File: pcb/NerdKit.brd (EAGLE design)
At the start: 148.3 x 69.8 mm, 31 parts, among them U2 ARDUINOR3-PINSONLY

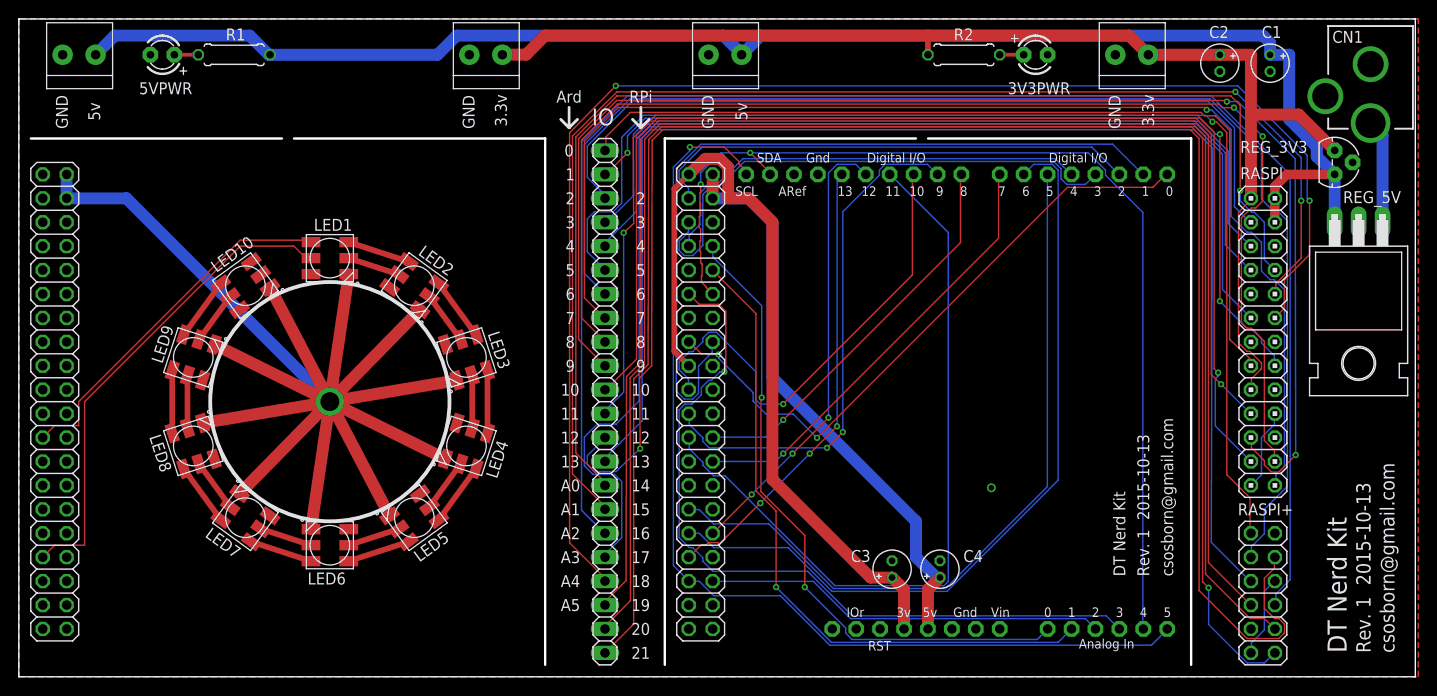
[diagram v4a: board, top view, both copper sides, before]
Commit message: Added OSH Park compliant cutouts for daughter cards.
See http://docs.oshpark.com/submitting-orders/cutouts-and-slots/.
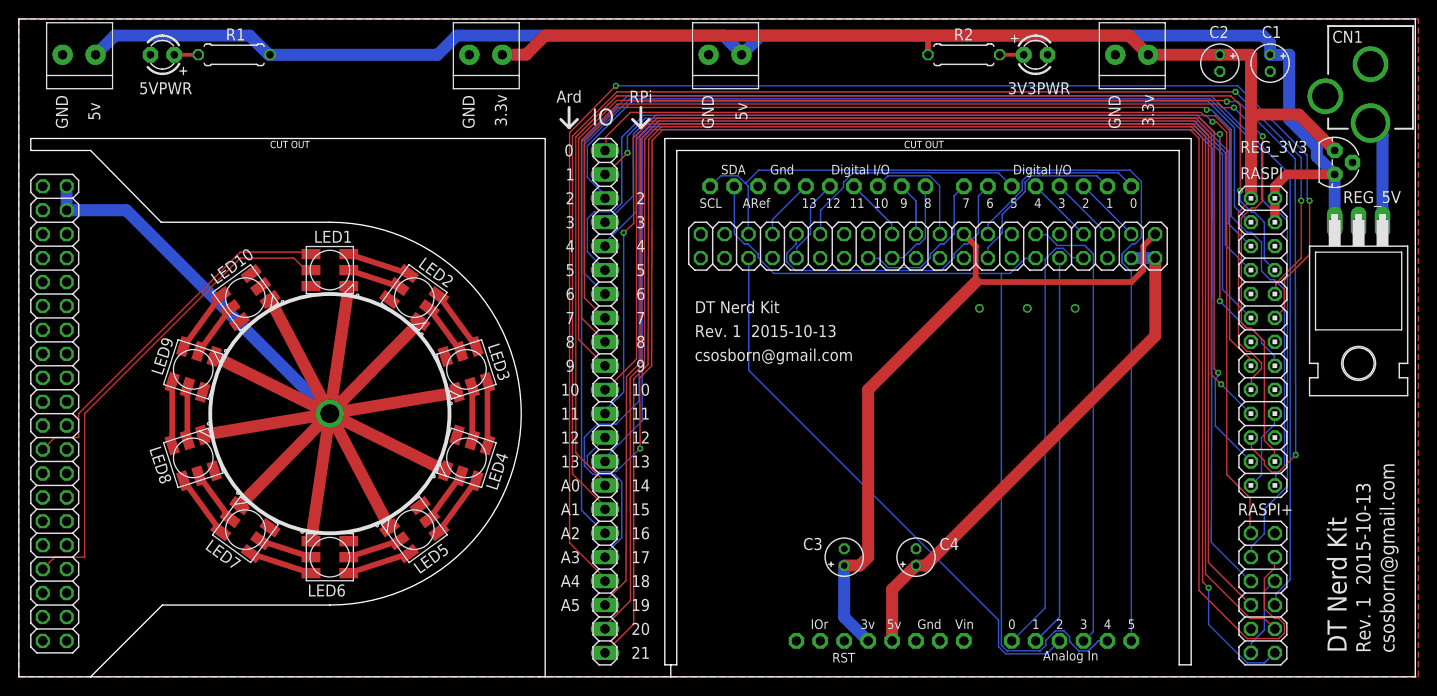
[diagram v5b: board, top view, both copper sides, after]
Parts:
- moved ARDUINOIO 29.2 mm to (96.5, 45.7), turned to 180 degrees
- moved C3 5.24 mm to (87.6, 12.7)
- moved U2 4.02 mm to (96.5, 27.9)
- moved C4 2.84 mm to (95.2, 12.7)
- moved LED1 1.27 mm to (33.0, 43.2)
- moved LED10 1.27 mm to (24.1, 40.3)
- moved LED2 1.27 mm to (42.0, 40.3)
- moved LED6 1.27 mm to (33.0, 12.7)
- moved ARDUINOIO1 1.27 mm to (3.81, 27.9)
- moved LED4 1.27 mm to (47.5, 23.2)
- moved LED8 1.27 mm to (18.5, 23.2)
- moved LED5 1.27 mm to (42.0, 15.6)
- moved LED7 1.27 mm to (24.1, 15.6)
- moved LED3 1.27 mm to (47.5, 32.6)
- moved LED9 1.27 mm to (18.5, 32.6)
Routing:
- net AR11: track 80.9 -> 6.78 mm
- net AR01: track 84.6 -> 19.2 mm
- net AR05: track 79.2 -> 25.4 mm
- net AR06: track 83.9 -> 31.3 mm
- net AR03: track 57.2 -> 7.19 mm
- net AR09: track 55.7 -> 5.71 mm, vias 2 -> 0
- net AR00: track 67.4 -> 19.7 mm, vias 2 -> 0
- net AR02: track 52.4 -> 7.19 mm
- net AR13: track 48.6 -> 6.56 mm, vias 3 -> 0
- net AR04: track 47.8 -> 7.18 mm
- net AR12: track 48.1 -> 9.09 mm, vias 3 -> 0
- net AR10: track 51.0 -> 12.6 mm, vias 1 -> 0
- net ARA3: track 82.6 -> 48.5 mm, vias 1 -> 0
- net AR08: track 42.2 -> 9.94 mm, vias 1 -> 0
- net AR07: track 47.0 -> 16.7 mm, vias 1 -> 0
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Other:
- outline, holes or cut-outs redrawn
- board text added: "CUT OUT"

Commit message: Ditched the 2.1mm DC jack and regulator in favor of micro USB for power.
This fixes #5.
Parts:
- removed CN1: (no value), adafruit:DCJACK_2MM_PTH
- removed REG_5V: 7805T, adafruit:TO220H
- added USB: FCI 10118194-0001LF, microbuilder:4UCONN_20329
- moved C1 18.6 mm to (138.4, 47.4)
- moved REG_3V3 4.32 mm to (137.7, 58.4)
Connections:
- removed net GNDBREAK: CN1.GNDBREAK
- removed net N$2: CN1.PWR, REG_5V.1
- net 5V: now also USB.VBUS; no longer REG_5V.3
- net GND: now also USB.BASE@1, USB.BASE@2, USB.GND, USB.SPRT@1, USB.SPRT@2, USB.SPRT@3, USB.SPRT@4; no longer CN1.GND, REG_5V.2
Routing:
- net N$2: track 11.1 -> 0.00 mm
- net 5V: track 163.5 -> 172.4 mm
- net 3V3: track 131.4 -> 126.4 mm
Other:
- outline, holes or cut-outs redrawn

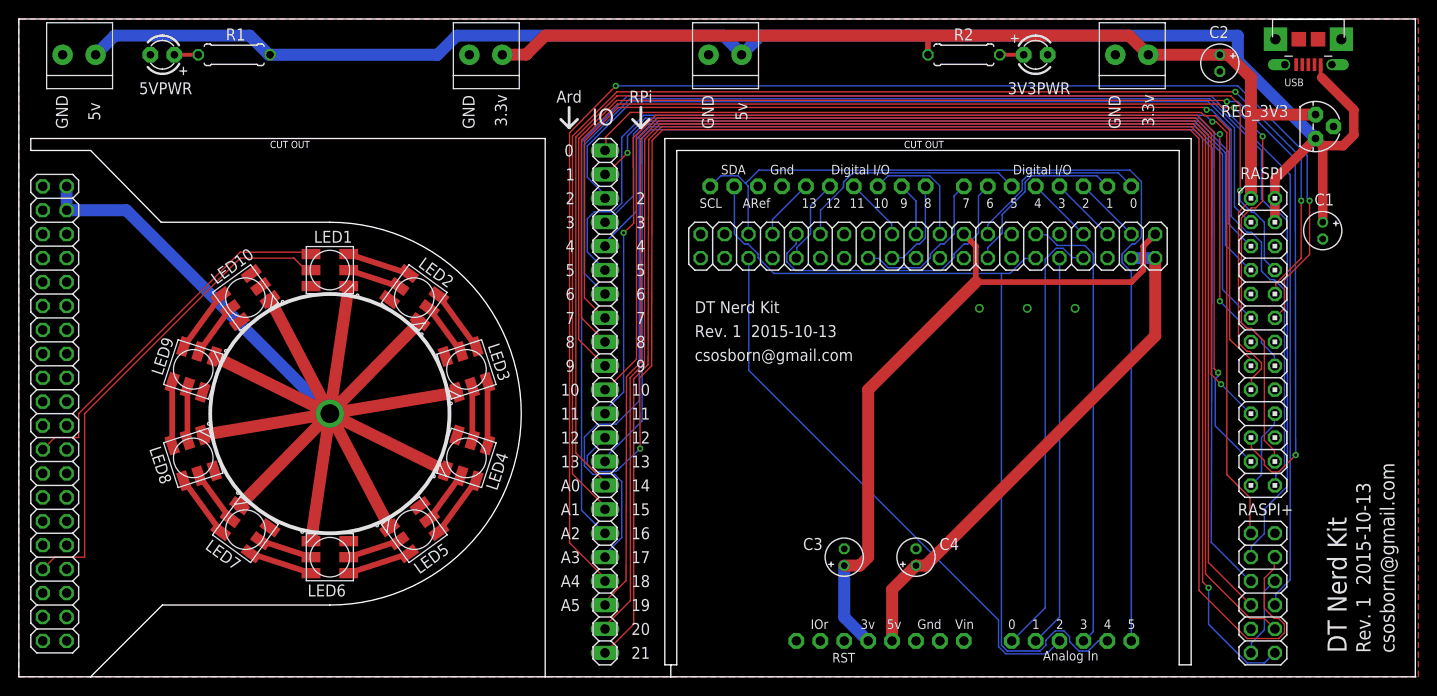
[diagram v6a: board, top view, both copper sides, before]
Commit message: Added mounting holes.
Also brought the USB D+ and D- signals out to test points, just for fun.
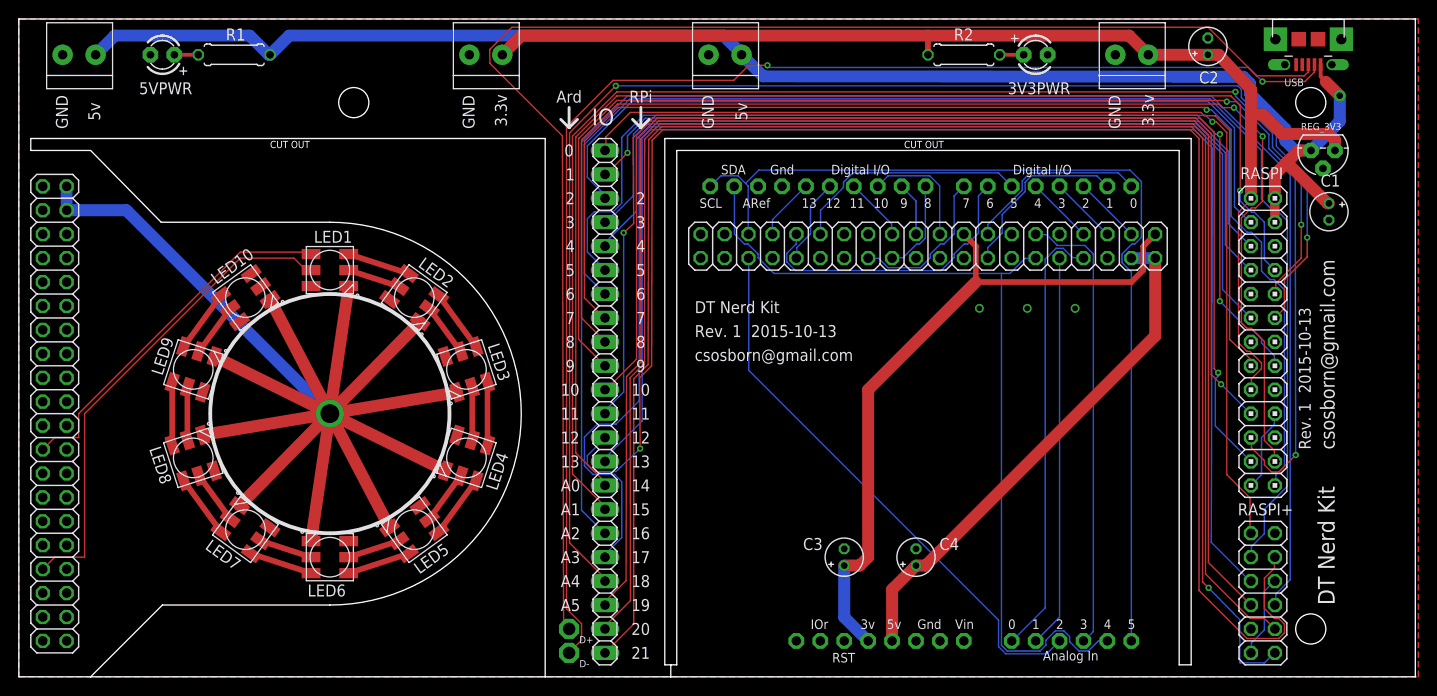
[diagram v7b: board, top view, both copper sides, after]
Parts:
- added D+, D-: TPPAD1-13, testpad:P1-13
- moved REG_3V3 2.66 mm to (138.5, 55.9), turned to 180 degrees
- moved C2 2.18 mm to (126.2, 66.9), turned to 90 degrees
- moved C1 2.11 mm to (139.1, 49.4)
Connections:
- new net N$2: D+.TP, USB.D+
- new net N$21: D-.TP, USB.D-
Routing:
- net N$2: track 0.00 -> 156.6 mm
- net N$21: track 0.00 -> 141.1 mm, vias 0 -> 2
- net 5V: track 172.4 -> 165.5 mm, vias 0 -> 1
- net 3V3: track 126.4 -> 130.0 mm

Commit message: Lots of trace cleanup and local optimizations.
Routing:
- net N$2: track 156.6 -> 137.9 mm, vias 0 -> 2
- net GND: track 17.4 -> 7.22 mm
- net 5V: track 165.5 -> 167.8 mm
- net GPIO15: track 139.0 -> 137.8 mm
- net GPIO18: track 151.3 -> 150.3 mm
- net GPIO22: track 95.6 -> 94.7 mm
- net GPIO02: track 89.0 -> 88.1 mm
- net GPIO13: track 145.5 -> 144.7 mm
- net GPIO23: track 96.8 -> 96.0 mm
- net GPIO05: track 127.1 -> 126.4 mm
- net GPIO17: track 134.1 -> 133.4 mm
- net GPIO06: track 139.1 -> 138.4 mm
- net GPIO14: track 130.2 -> 129.5 mm
- net GPIO04: track 91.1 -> 90.4 mm
- net N$21: track 141.1 -> 140.4 mm
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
